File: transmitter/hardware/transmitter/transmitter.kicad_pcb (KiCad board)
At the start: 2 copper layers, 56 x 47 mm, 33 parts, among them J1 SOIL, J2 SOIL, J3 USB_UART, J4 PWR, J5 SOIL, J6 SOIL, J7 SOIL, J8 SOIL, SW1 SW_SPST, SW2 SW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

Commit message: Start of placement
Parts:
- removed F1: Polyfuse, Fuse:Fuse_1812_4532Metric_Pad1.30x3.40mm_HandSolder
- removed G***: LOGO, theapi:sunflower
- removed REF** (x2): TheApiLogoTiny, theapi:TheApiLogoTiny
- removed REF**: TheApiLogo, theapi:TheApiLogoSmall
- added C7: 1000pF, Capacitor_SMD:C_0603_1608Metric_Pad1.05x0.95mm_HandSolder, F.Cu at (192.3, 75.9)
- added Q1: Si2305CDS, Package_TO_SOT_SMD:SOT-23, F.Cu at (141.2, 86.7)
- added Q2: BSS138, Package_TO_SOT_SMD:SOT-23, F.Cu at (141.3, 82.6)
- added Q3: Si2305CDS, Package_TO_SOT_SMD:SOT-23, F.Cu at (132.4, 102.4)
- added Q4: BSS138, Package_TO_SOT_SMD:SOT-23, F.Cu at (127.9, 102.5)
- added R10: 10K, Resistor_SMD:R_0603_1608Metric_Pad1.05x0.95mm_HandSolder, F.Cu at (199.2, 72.3)
- added R11: 10K, Resistor_SMD:R_0603_1608Metric_Pad1.05x0.95mm_HandSolder, F.Cu at (204.0, 68.7)
- added R12: 10K, Resistor_SMD:R_0603_1608Metric_Pad1.05x0.95mm_HandSolder, F.Cu at (199.2, 73.8)
- added R13: 100K, Resistor_SMD:R_0603_1608Metric_Pad1.05x0.95mm_HandSolder, F.Cu at (199.0, 75.9)
- added R14: 10K, Resistor_SMD:R_0603_1608Metric_Pad1.05x0.95mm_HandSolder, F.Cu at (204.0, 70.2)
- added R9: 10K, Resistor_SMD:R_0603_1608Metric_Pad1.05x0.95mm_HandSolder, F.Cu at (195.6, 75.9)
- added U5: BD4833G, Package_TO_SOT_SMD:SOT-23-5_HandSoldering, F.Cu at (124.5, 96.7)
- C1: value 0.1uf -> 0.1uF
- C4: value 1uF -> 0.1uF
- SW1: value SW_SPST -> SW_Push; footprint Connector_PinHeader_2.54mm:PinHeader_1x02_P2.54mm_Vertical -> Button_Switch_THT:SW_Tactile_Straight_KSL0Axx1LFTR
- U2: value MCP1700-3302E_SOT89 -> tpl5111; footprint Package_TO_SOT_SMD:SOT-89-3 -> Package_TO_SOT_SMD:SuperSOT-6
- U4: value MCP1703A-3302_SOT223 -> tps73733; footprint Package_TO_SOT_SMD:SOT-223-3_TabPin2 -> Package_TO_SOT_SMD:SOT-223-6
- moved C4 50.4 mm to (92.9, 106.0)
- moved C6 49.8 mm to (105.9, 106.5)
- moved U2 25.0 mm to (118.1, 96.1)
- moved U4 11.3 mm to (144.4, 103.9), turned to 270 degrees
- moved C5 10.9 mm to (149.9, 114.7)
- moved SW1 10.0 mm to (124.3, 108.6)
- moved C3 9.60 mm to (142.5, 113.9)
- moved R2 4.58 mm to (152.0, 103.7)
- moved R1 4.52 mm to (152.0, 101.9)
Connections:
- C1 pad 1: SENSE_PWR -> 3V3
- C2 pad 1: SENSE_PWR -> 3V3
- C3 pad 1: /PWR -> /VBAT
- C4 pad 1: 3V3 -> /VBAT
- C5 pad 1: /PWR -> 3V3
- C6 pad 1: 3V3 -> /OUT+
- R1 pad 1: /PWR -> Net-(Q1-Pad3)
- R3 pad 1: SENSE_PWR -> 3V3
- R4 pad 1: SENSE_PWR -> 3V3
- R5 pad 1: SENSE_PWR -> 3V3
- R6 pad 1: SENSE_PWR -> 3V3
- R7 pad 1: SENSE_PWR -> 3V3
- R8 pad 1: SENSE_PWR -> 3V3
- SW1 pad 1: RESET -> /VBAT
- SW1 pad 2: Net-(SW1-Pad2) -> Net-(R13-Pad2)
- SW2 pad 2: /PWR -> /VBAT
- U1 pad 13: RESET -> (no net)
- U1 pad 15: /PWR -> /VBAT
- U1 pad 29: SENSE_PWR -> DONE
- U1 pad 30: Net-(SW1-Pad2) -> (no net)
- U2 pad 1: GND -> /VBAT
- U2 pad 2: /PWR -> GND
- U2 pad 3: 3V3 -> Net-(R13-Pad2)
- U3 pad 16: SENSE_PWR -> 3V3
- U4 pad 1: /PWR -> /VBAT
- U4 pad 2: GND -> 3V3
- U4 pad 3: 3V3 -> GND
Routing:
- net Net-(SW1-Pad2): track 55.6 -> 0.00 mm, vias 1 -> 0
- net SENSE_PWR: track 38.2 -> 0.00 mm
- net /PWR: track 36.0 -> 0.00 mm
- net 3V3: track 63.5 -> 96.0 mm
- net /OUT+: track 23.1 -> 0.00 mm
- net RESET: track 6.70 -> 0.00 mm
- net /VBAT: track 0.00 -> 6.38 mm
- net Net-(Q3-Pad3): track 5.99 -> 0.00 mm
- net GND: track 28.0 -> 22.5 mm
- net BATT_SENSE: track 20.6 -> 18.8 mm
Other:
- board text removed: "SLEEP"

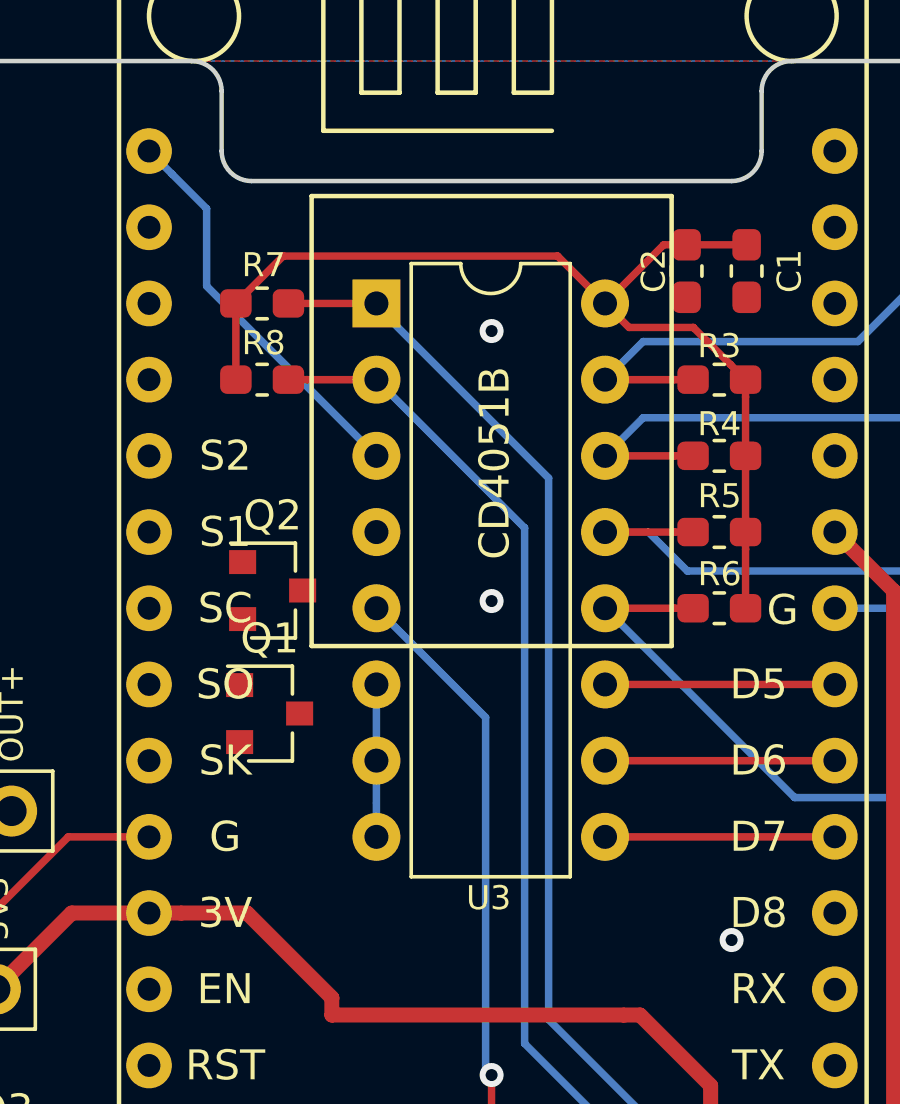
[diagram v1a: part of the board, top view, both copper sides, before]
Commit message: Smaller multiplexer
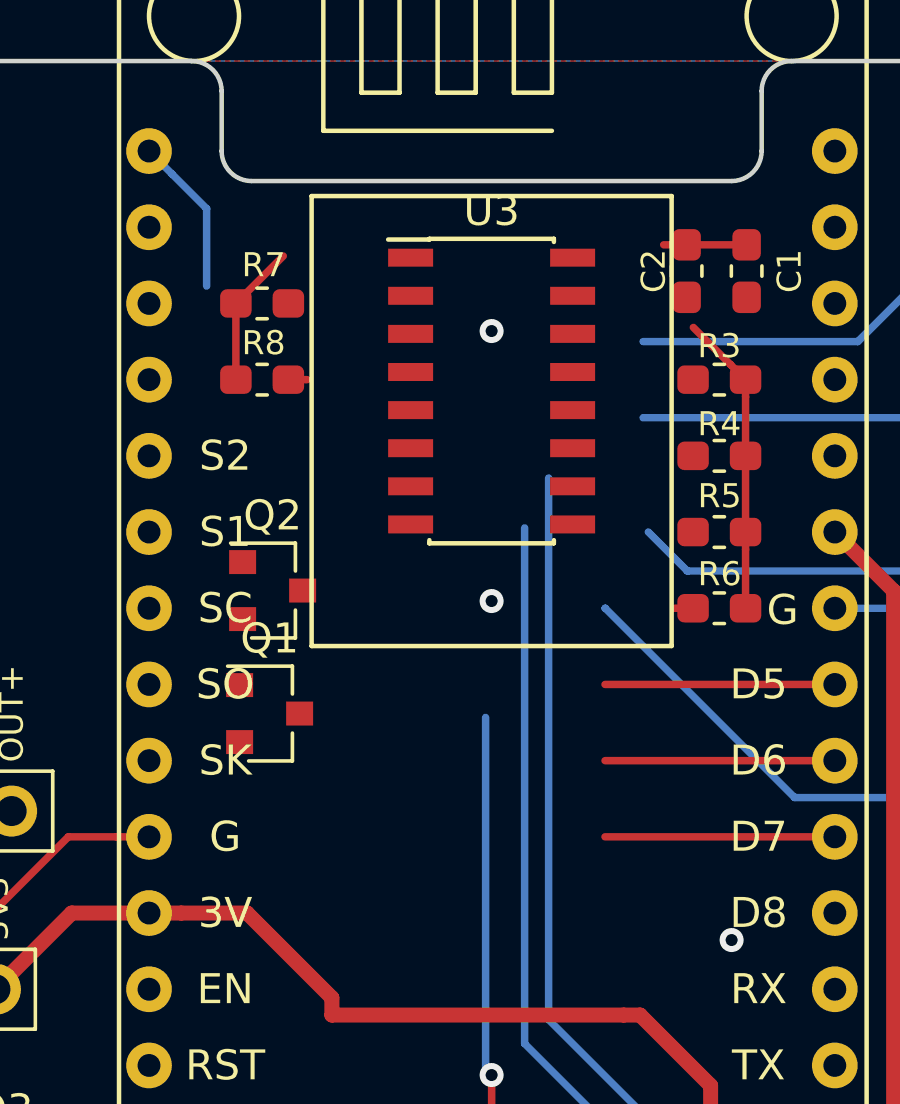
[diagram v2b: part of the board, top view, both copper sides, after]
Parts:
- U3: footprint Package_DIP:DIP-16_W7.62mm -> Package_SO:SOIC-16_3.9x9.9mm_P1.27mm
- moved U3 4.82 mm to (148.6, 75.9)
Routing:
- net 3V3: track 96.0 -> 78.6 mm
- net SOIL_5: track 53.1 -> 41.9 mm
- net SOIL_6: track 48.0 -> 38.7 mm
- net A0: track 13.3 -> 5.30 mm
- net BATT_SENSE: track 18.8 -> 13.7 mm
- net GND: track 22.5 -> 17.4 mm
- net SOIL_2: track 18.8 -> 14.0 mm
- net SOIL_1: track 20.9 -> 16.1 mm
- net SOIL_3: track 18.8 -> 14.4 mm
- net SOIL_4: track 20.9 -> 18.6 mm

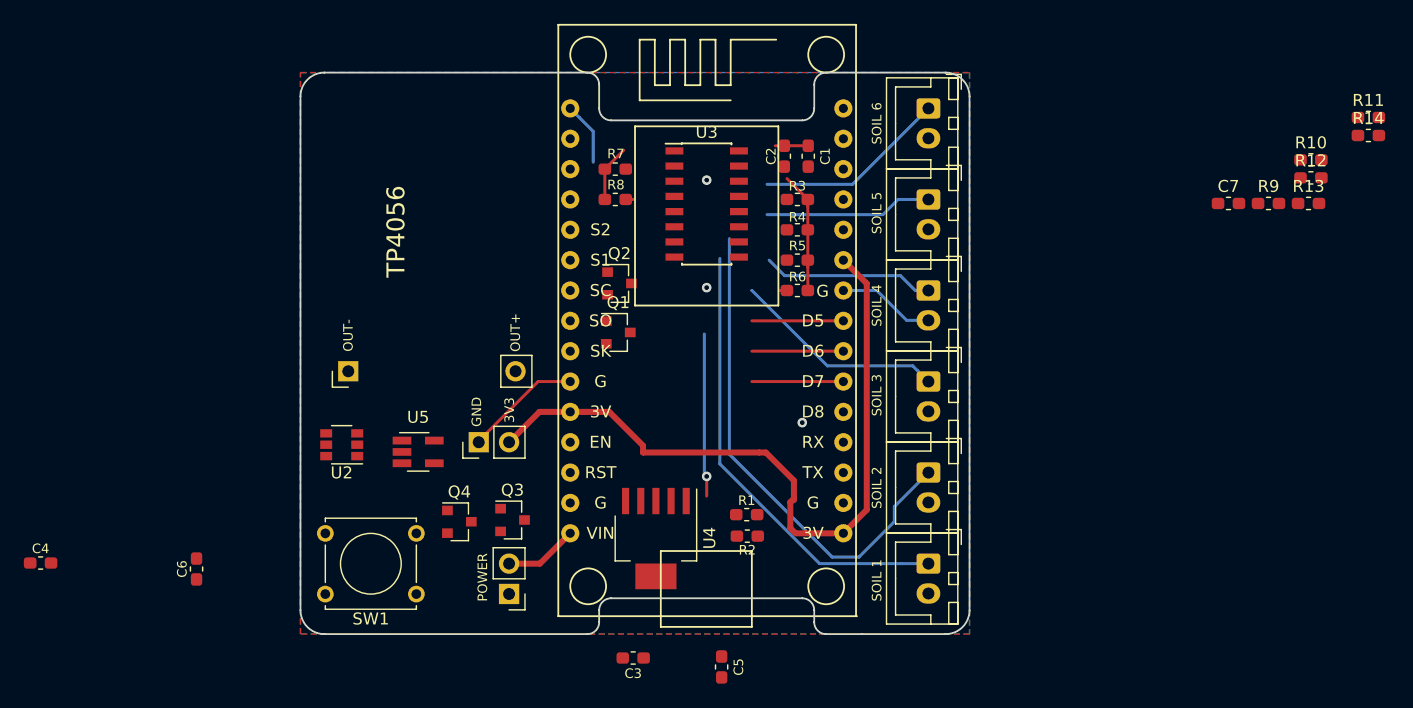
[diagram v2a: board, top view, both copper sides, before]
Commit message: Wired multiplexer
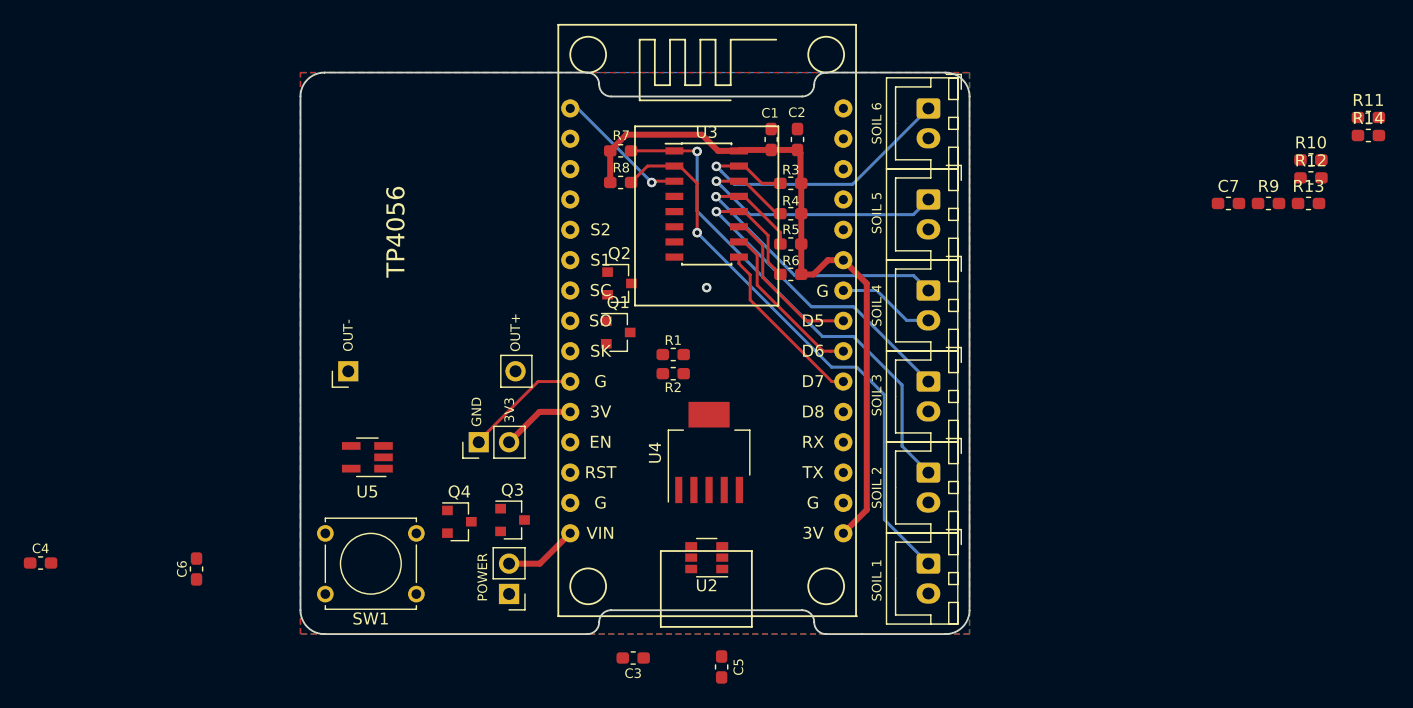
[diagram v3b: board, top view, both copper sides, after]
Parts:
- moved U2 32.0 mm to (148.6, 105.5)
- moved R2 14.9 mm to (145.8, 90.1)
- moved R1 14.7 mm to (145.8, 88.5)
- moved U4 8.46 mm to (148.8, 96.7), turned to 90 degrees
- moved U5 4.27 mm to (120.2, 97.1), turned to 180 degrees
- moved C1 3.40 mm to (154.0, 70.5), turned to 90 degrees
- moved C2 1.78 mm to (156.2, 70.5), turned to 90 degrees
- moved R7 1.59 mm to (141.4, 71.5)
- moved R8 1.49 mm to (141.4, 74.1)
- moved R4 1.46 mm to (155.7, 76.8)
- moved R6 1.46 mm to (155.7, 81.8)
- moved R3 1.46 mm to (155.7, 74.2)
- moved R5 1.46 mm to (155.7, 79.3)
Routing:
- net SOIL_3: track 14.4 -> 28.6 mm, vias 0 -> 1
- net SOIL_4: track 18.6 -> 32.5 mm, vias 0 -> 1
- net 3V3: track 78.6 -> 64.7 mm
- net BATT_SENSE: track 13.7 -> 0.00 mm, vias 1 -> 0
- net SOIL_2: track 14.0 -> 25.9 mm, vias 0 -> 1
- net SOIL_1: track 16.1 -> 27.0 mm, vias 0 -> 1
- net SOIL_6: track 38.7 -> 47.8 mm, vias 0 -> 1
- net Net-(U1-Pad21): track 7.66 -> 14.6 mm
- net A0: track 5.30 -> 11.8 mm, vias 0 -> 1
- net Net-(U1-Pad22): track 7.66 -> 14.0 mm
- net Net-(U1-Pad23): track 7.66 -> 13.6 mm
- net SOIL_5: track 41.9 -> 42.0 mm, vias 0 -> 1
- net GND: vias 3 -> 1
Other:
- outline, holes or cut-outs redrawn

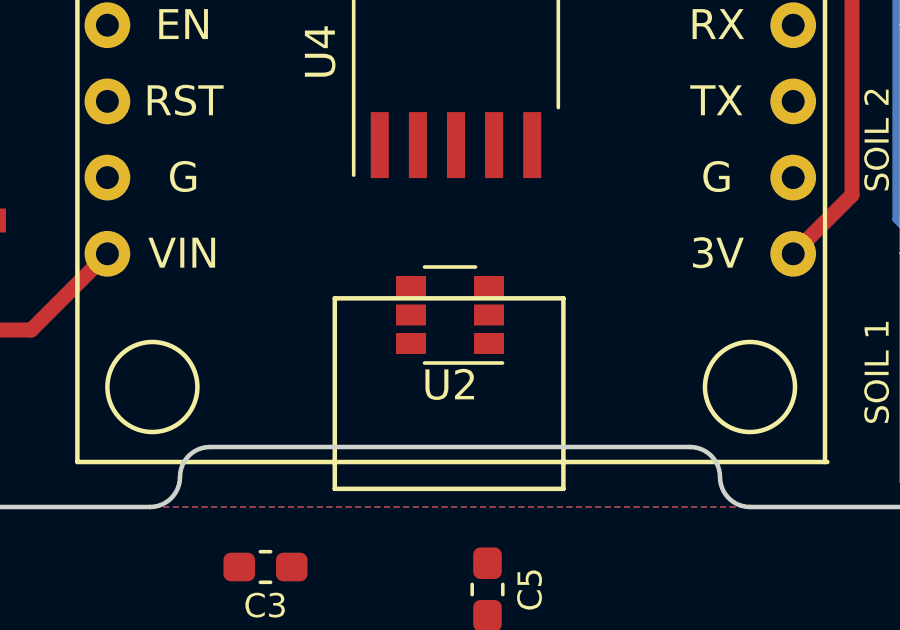
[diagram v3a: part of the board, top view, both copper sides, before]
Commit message: TPL5111 footprint
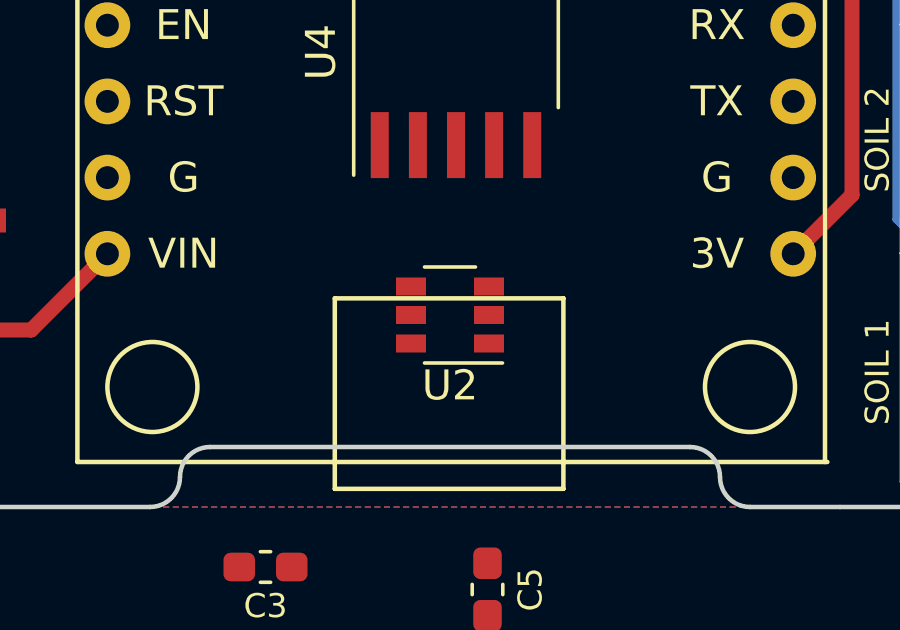
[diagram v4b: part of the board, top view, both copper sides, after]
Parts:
- U2: footprint Package_TO_SOT_SMD:SuperSOT-6 -> tpl511x:SOT-6-DDC
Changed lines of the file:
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@@
     (add_net 3V3)
+  )
+  (module tpl511x:SOT-6-DDC (layer F.Cu)
+    (at 148.62 105.545 180)
+    (descr "6-pin SuperSOT package http://www.mouser.com/ds/2/149/FMB5551-889214.pdf")
+    (tags "SuperSOT-6 SSOT-6")
+    (attr smd)
+    (fp_text reference U2 (at 0 -2.35 180) (layer F.SilkS)
+      (effects (font (size 1 1) (thickness 0.15)))
+    )
+    (fp_text value tpl5111 (at 0 2.5 180) (layer F.Fab)
+      (effects (font (size 1 1) (thickness 0.15)))
+    )
+    (fp_line (start 2.05 1.7) (end -2.05 1.7) (layer F.CrtYd) (width 0.05))
+    (fp_line (start 2.05 1.7) (end 2.05 -1.7) (layer F.CrtYd) (width 0.05))
+    (fp_line (start -2.05 -1.7) (end -2.05 1.7) (layer F.CrtYd) (width 0.05))
+    (fp_line (start -2.05 -1.7) (end 2.05 -1.7) (layer F.CrtYd) (width 0.05))
+    (fp_line (start -0.85 -1) (end -0.85 1.45) (layer F.Fab) (width 0.12))
+    (fp_line (start -0.4 -1.45) (end -0.85 -1) (layer F.Fab) (width 0.12))
+    (fp_line (start 0.85 -1.45) (end -0.4 -1.45) (layer F.Fab) (width 0.12))
+    (fp_line (start 0.85 1.45) (end 0.85 -1.45) (layer F.Fab) (width 0.12))
+    (fp_line (start -0.85 1.45) (end 0.85 1.45) (layer F.Fab) (width 0.12))
+    (fp_line (start 0.85 1.6) (end -0.85 1.6) (layer F.SilkS) (width 0.12))
+    (fp_line (start 0.85 -1.6) (end -1.75 -1.6) (layer F.SilkS) (width 0.12))
+    (fp_text user %R (at 0 0 270) (layer F.Fab)
+      (effects (font (size 0.5 0.5) (thickness 0.075)))
+    )
+    (pad 5 smd rect (at 1.3 0 180) (size 1 0.6) (layers F.Cu F.Paste F.Mask)
+      (net 24 "Net-(U2-Pad5)"))
+    (pad 6 smd rect (at 1.3 -0.95 180) (size 1 0.6) (layers F.Cu F.Paste F.Mask)
+      (net 15 /VBAT))
+    (pad 4 smd rect (at 1.3 0.95 180) (size 1 0.6) (layers F.Cu F.Paste F.Mask)
+      (net 23 DONE))
+    (pad 3 smd rect (at -1.3 0.95 180) (size 1 0.6) (layers F.Cu F.Paste F.Mask)
+      (net 22 "Net-(R13-Pad2)"))
+    (pad 2 smd rect (at -1.3 0 180) (size 1 0.6) (layers F.Cu F.Paste F.Mask)
+      (net 1 GND))
+    (pad 1 smd rect (at -1.3 -0.95 180) (size 1 0.6) (layers F.Cu F.Paste F.Mask)
+      (net 15 /VBAT))
+    (model ${KISYS3DMOD}/Package_TO_SOT_SMD.3dshapes/SuperSOT-6.wrl
+      (at (xyz 0 0 0))
+      (scale (xyz 1 1 1))
+      (rotate (xyz 0 0 0))
+    )
   )
   (module "ESP8266:NodeMCU1.0(12-E)" (layer F.Cu)
@@
       (at (xyz 0 0 0))
       (scale (xyz 1 1 1))
-      (rotate (xyz 0 0 0))
-    )
-  )
-  (module Package_TO_SOT_SMD:SuperSOT-6 (layer F.Cu)
-    (at 148.62 105.545 180)
-    (descr "6-pin SuperSOT package http://www.mouser.com/ds/2/149/FMB5551-889214.pdf")
-    (tags "SuperSOT-6 SSOT-6")
-    (attr smd)
-    (fp_text reference U2 (at 0 -2.35 180) (layer F.SilkS)
-      (effects (font (size 1 1) (thickness 0.15)))
-    )
-    (fp_text value tpl5111 (at 0 2.5 180) (layer F.Fab)
-      (effects (font (size 1 1) (thickness 0.15)))
-    )
-    (fp_line (start 2.05 1.7) (end -2.05 1.7) (layer F.CrtYd) (width 0.05))
-    (fp_line (start 2.05 1.7) (end 2.05 -1.7) (layer F.CrtYd) (width 0.05))
-    (fp_line (start -2.05 -1.7) (end -2.05 1.7) (layer F.CrtYd) (width 0.05))
-    (fp_line (start -2.05 -1.7) (end 2.05 -1.7) (layer F.CrtYd) (width 0.05))
-    (fp_line (start -0.85 -1) (end -0.85 1.45) (layer F.Fab) (width 0.12))
-    (fp_line (start -0.4 -1.45) (end -0.85 -1) (layer F.Fab) (width 0.12))
-    (fp_line (start 0.85 -1.45) (end -0.4 -1.45) (layer F.Fab) (width 0.12))
-    (fp_line (start 0.85 1.45) (end 0.85 -1.45) (layer F.Fab) (width 0.12))
-    (fp_line (start -0.85 1.45) (end 0.85 1.45) (layer F.Fab) (width 0.12))
-    (fp_line (start 0.85 1.6) (end -0.85 1.6) (layer F.SilkS) (width 0.12))
-    (fp_line (start 0.85 -1.6) (end -1.75 -1.6) (layer F.SilkS) (width 0.12))
-    (fp_text user %R (at 0 0 270) (layer F.Fab)
-      (effects (font (size 0.5 0.5) (thickness 0.075)))
-    )
-    (pad 5 smd rect (at 1.3 0 180) (size 1 0.7) (layers F.Cu F.Paste F.Mask)
-      (net 24 "Net-(U2-Pad5)"))
-    (pad 6 smd rect (at 1.3 -0.95 180) (size 1 0.7) (layers F.Cu F.Paste F.Mask)
-      (net 15 /VBAT))
-    (pad 4 smd rect (at 1.3 0.95 180) (size 1 0.7) (layers F.Cu F.Paste F.Mask)
-      (net 23 DONE))
-    (pad 3 smd rect (at -1.3 0.95 180) (size 1 0.7) (layers F.Cu F.Paste F.Mask)
-      (net 22 "Net-(R13-Pad2)"))
-    (pad 2 smd rect (at -1.3 0 180) (size 1 0.7) (layers F.Cu F.Paste F.Mask)
-      (net 1 GND))
-    (pad 1 smd rect (at -1.3 -0.95 180) (size 1 0.7) (layers F.Cu F.Paste F.Mask)
-      (net 15 /VBAT))
-    (model ${KISYS3DMOD}/Package_TO_SOT_SMD.3dshapes/SuperSOT-6.wrl
-      (at (xyz 0 0 0))
-      (scale (xyz 1 1 1))
